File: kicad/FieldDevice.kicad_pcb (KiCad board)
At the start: 2 copper layers, 53.5 x 38.5 mm, 36 parts, among them P201 Positive, P202 Negative, P301 CONN_01X06, SW301 SW_PUSH, U101 DS7505

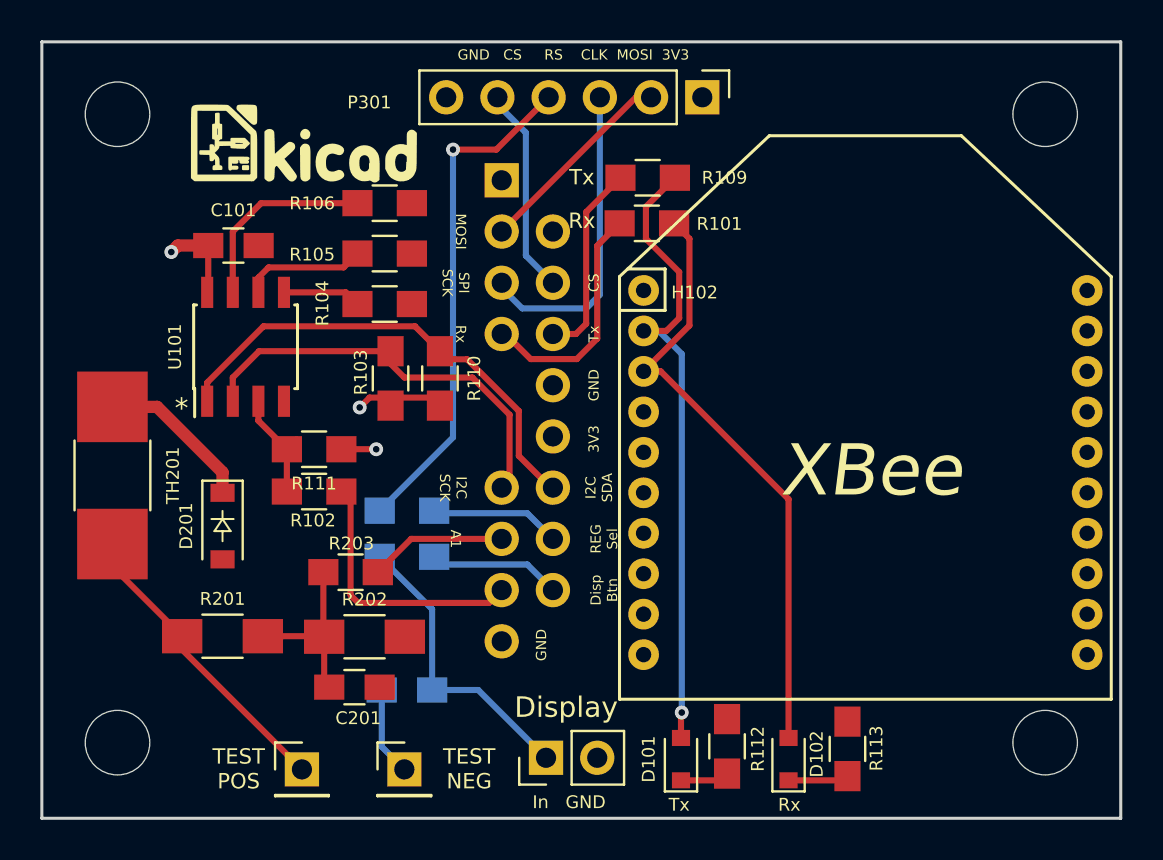
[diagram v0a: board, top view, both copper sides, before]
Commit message: Started some changes to model a tank for a demo
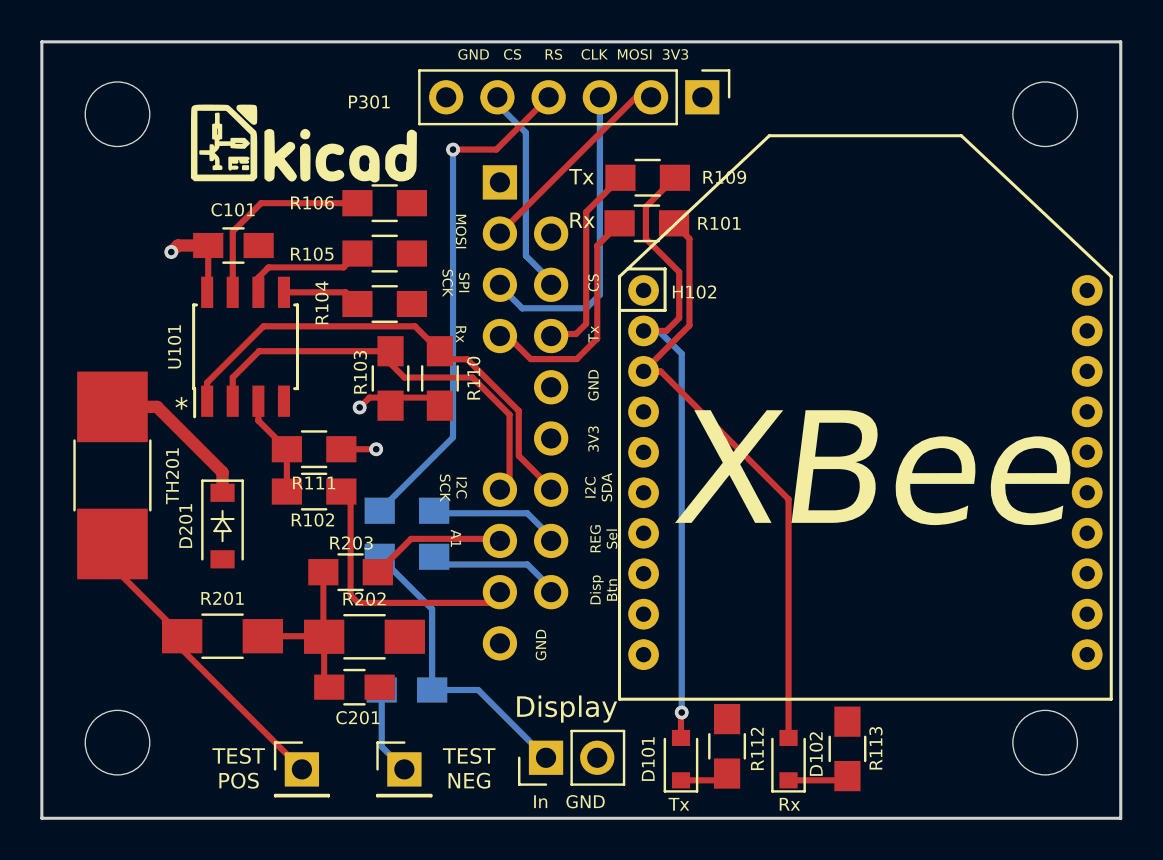
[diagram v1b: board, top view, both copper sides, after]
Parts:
- moved H101 0.13 mm to (132.8, 71.0)
